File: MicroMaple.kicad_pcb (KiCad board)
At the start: 2 copper layers, 38.1 x 38.1 mm, 45 parts, among them P1 USB_OTG, P2 CONN_01X14, P3 CONN_01X14, P4 CONN_01X12, P5 CONN_01X01, P6 CONN_01X01, P7 CONN_01X01, P8 CONN_01X01, Q1 8050, Q2 8050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

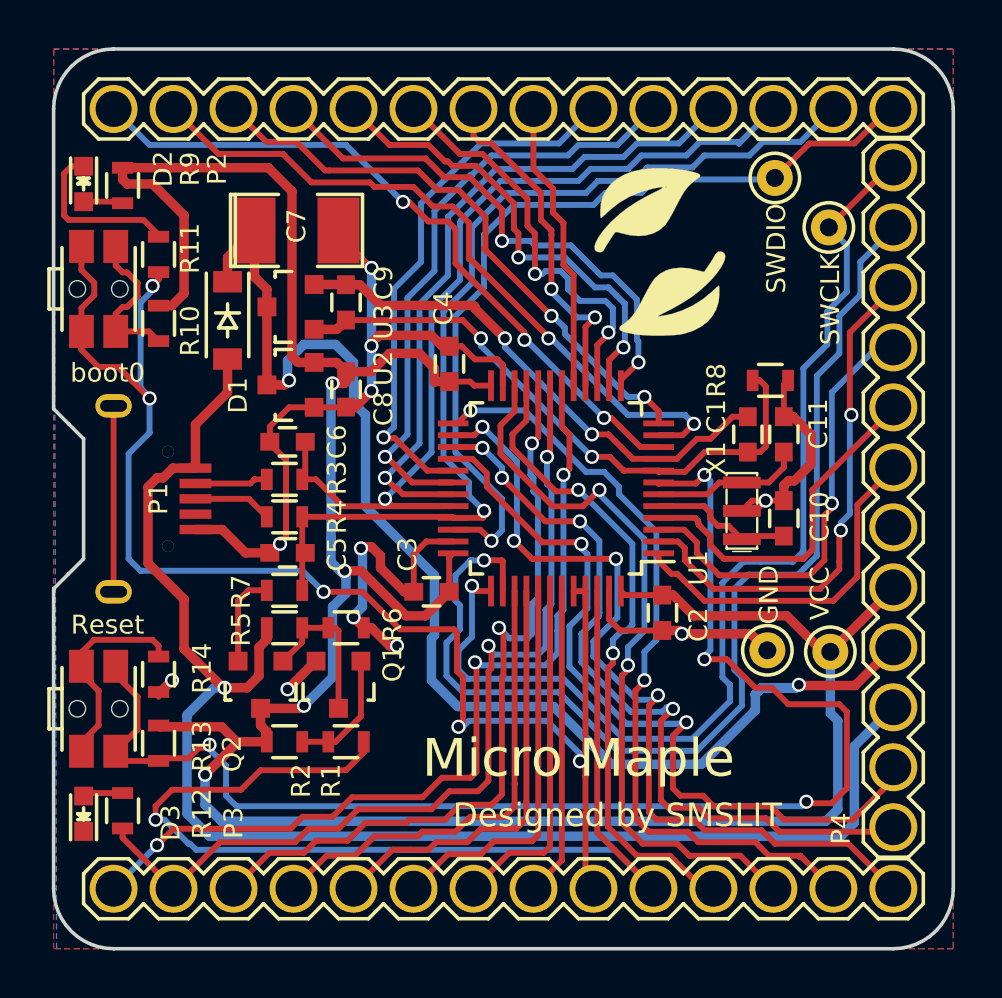
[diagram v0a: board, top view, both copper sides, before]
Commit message: 1.remove the USB disconnect circuit. 2.export v1.1 pdf. 3.add smslit logo lib
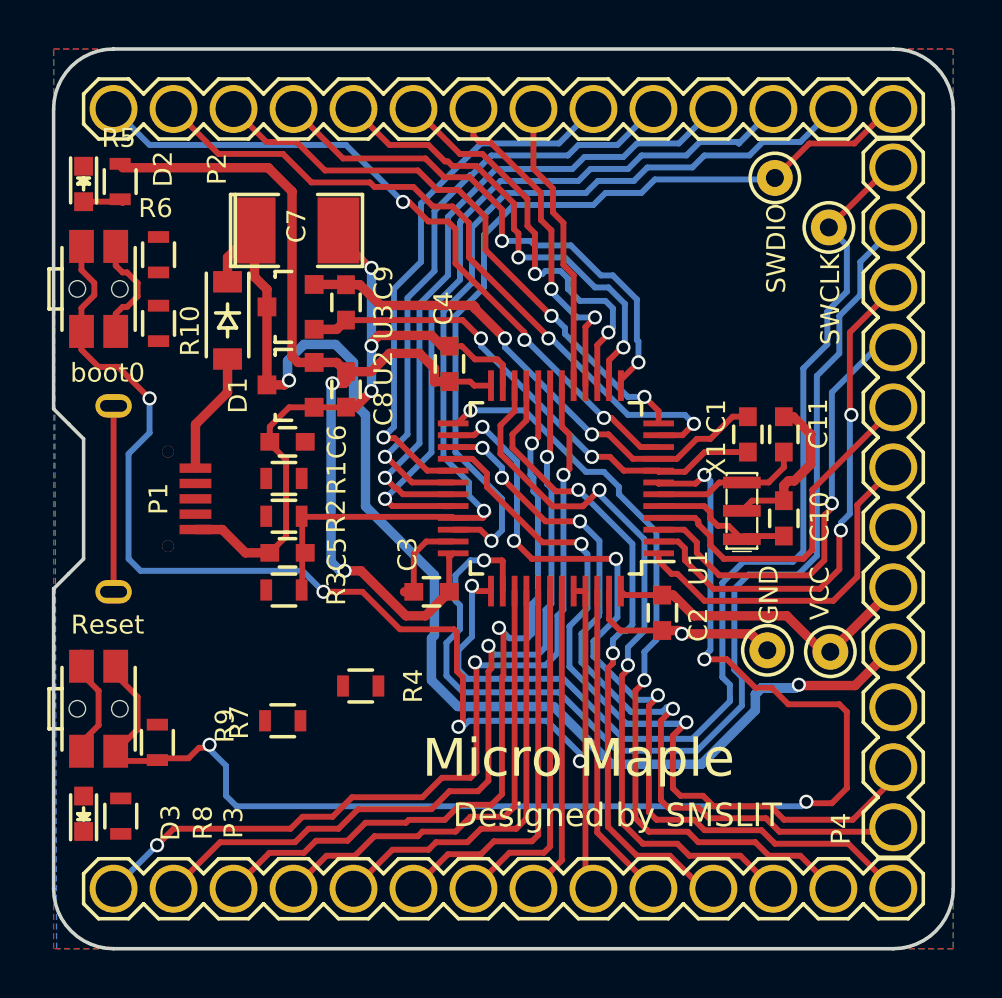
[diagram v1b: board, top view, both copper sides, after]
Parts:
- removed G***: LOGO, myFootprints:logo
- removed Q1, Q2: 8050, TO_SOT_Packages_SMD:SOT-23
- removed R11, R13: 10K, Resistors_SMD:R_0603
- removed R12, R14: 1K, Resistors_SMD:R_0603
- R1: value 1K -> 22
- R2: value 47K -> 22
- R3: value 22 -> 1.5K
- R4: value 22 -> 0
- R5: value 10K -> 1K
- R6: value 36K -> 1K
- R7: value 1.5K -> 10K
- R8: value 0 -> 1K
- R9: value 1K -> 10K
- moved R8 33.1 mm to (132.4, 123.9), turned to 270 degrees
- moved R9 23.6 mm to (133.9, 120.8)
- moved R5 20.1 mm to (132.4, 97.1), turned to 90 degrees
- moved R6 17.7 mm to (134.0, 100.2), turned to 270 degrees
- moved R1 11.5 mm to (139.3, 109.6)
- moved R2 9.55 mm to (139.3, 111.2)
- moved R4 7.86 mm to (142.5, 118.4)
- moved R7 5.53 mm to (139.2, 119.9)
- moved R3 4.69 mm to (139.3, 114.4)
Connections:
- R1 pad 1: /PB9 -> /PA11
- R1 pad 2: Net-(Q1-Pad1) -> Net-(P1-Pad2)
- R10 pad 1: VCC -> Net-(R10-Pad1)
- R10 pad 2: Net-(R10-Pad2) -> GND
- R2 pad 1: Net-(Q1-Pad1) -> /PA12
- R2 pad 2: VCC -> Net-(P1-Pad3)
- R3 pad 1: /PA11 -> /PA12
- R3 pad 2: Net-(P1-Pad2) -> VCC
- R4 pad 1: /PA12 -> GND
- R4 pad 2: Net-(P1-Pad3) -> GNDA
- R5 pad 1: Net-(Q1-Pad3) -> Net-(D2-Pad2)
- R5 pad 2: +5V -> VCC
- R6 pad 1: GND -> VCC
- R6 pad 2: Net-(Q1-Pad3) -> Net-(R6-Pad2)
- R7 pad 1: /PA12 -> GND
- R7 pad 2: Net-(Q2-Pad2) -> /PB8
- R8 pad 1: GND -> Net-(D3-Pad2)
- R8 pad 2: GNDA -> /PB1
- R9 pad 1: Net-(D2-Pad2) -> /RST
- SW1 pad 1: Net-(R10-Pad2) -> Net-(R6-Pad2)
- SW2 pad 2: Net-(R14-Pad1) -> Net-(R10-Pad1)
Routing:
- net VCC: track 116.0 -> 55.5 mm, vias 4 -> 2
- net +5V: track 63.4 -> 6.62 mm, vias 1 -> 0
- net /PB9: track 47.0 -> 13.6 mm, vias 1 -> 0
- net GND: track 70.3 -> 48.8 mm, vias 11 -> 4
- net Net-(R14-Pad1): track 8.84 -> 0.00 mm
- net /PA11: track 40.1 -> 31.9 mm
- net Net-(Q1-Pad3): track 6.62 -> 0.00 mm
- net Net-(R10-Pad2): track 6.58 -> 0.00 mm
- net /PB8: track 61.2 -> 54.8 mm, vias 5 -> 4
- net Net-(Q1-Pad1): track 5.27 -> 0.00 mm
- net Net-(R10-Pad1): track 0.00 -> 4.79 mm
- net Net-(R6-Pad2): track 0.00 -> 4.59 mm
- net GNDA: track 25.8 -> 21.8 mm
- net Net-(Q2-Pad2): track 3.96 -> 0.00 mm
- net /PB1: track 39.1 -> 35.6 mm
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
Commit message: add the pinmap xlsx file and encorrect the Bsilks text for pins.
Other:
- board text added: "PB15 MOSI2"
- board text added: "PB6/PWM/SCL1"
- board text added: "PB7/PWM/SDA1"
- board text removed: "PB15 MISO2"
- board text removed: "PB6/PWM/SDA1"
- board text removed: "PB7/PWM/SCL1"
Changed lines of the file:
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@@
     (links 111)
     (no_connects 24)
-    (area 120.826799 86.2 178.03 129.615001)
+    (area 129.464999 91.364999 167.715001 129.615001)
     (thickness 1.6)
     (drawings 185)
@@
     (34 B.Paste user)
     (35 F.Paste user)
-    (36 B.SilkS user hide)
+    (36 B.SilkS user)
     (37 F.SilkS user)
     (38 B.Mask user)
@@
   (gr_line (start 155.702 119.507) (end 158.877 122.682) (angle 90) (layer B.SilkS) (width 0.2))
   (gr_line (start 155.702 112.268) (end 155.702 119.507) (angle 90) (layer B.SilkS) (width 0.2))
-  (gr_text "PB15\nMISO2" (at 160.147 120.142 90) (layer B.SilkS)
+  (gr_text "PB15\nMOSI2" (at 160.147 120.142 90) (layer B.SilkS)
     (effects (font (size 0.8 0.8) (thickness 0.12)) (justify mirror))
   )
@@
     (effects (font (size 0.8 0.8) (thickness 0.12)) (justify mirror))
   )
-  (gr_text PB7/PWM/SCL1 (at 142.24 114.808 90) (layer B.SilkS)
+  (gr_text PB7/PWM/SDA1 (at 142.24 114.808 90) (layer B.SilkS)
     (effects (font (size 0.8 0.8) (thickness 0.12)) (justify mirror))
   )
-  (gr_text PB6/PWM/SDA1 (at 139.7 114.808 90) (layer B.SilkS)
+  (gr_text PB6/PWM/SCL1 (at 139.7 114.808 90) (layer B.SilkS)
     (effects (font (size 0.8 0.8) (thickness 0.12)) (justify mirror))
   )

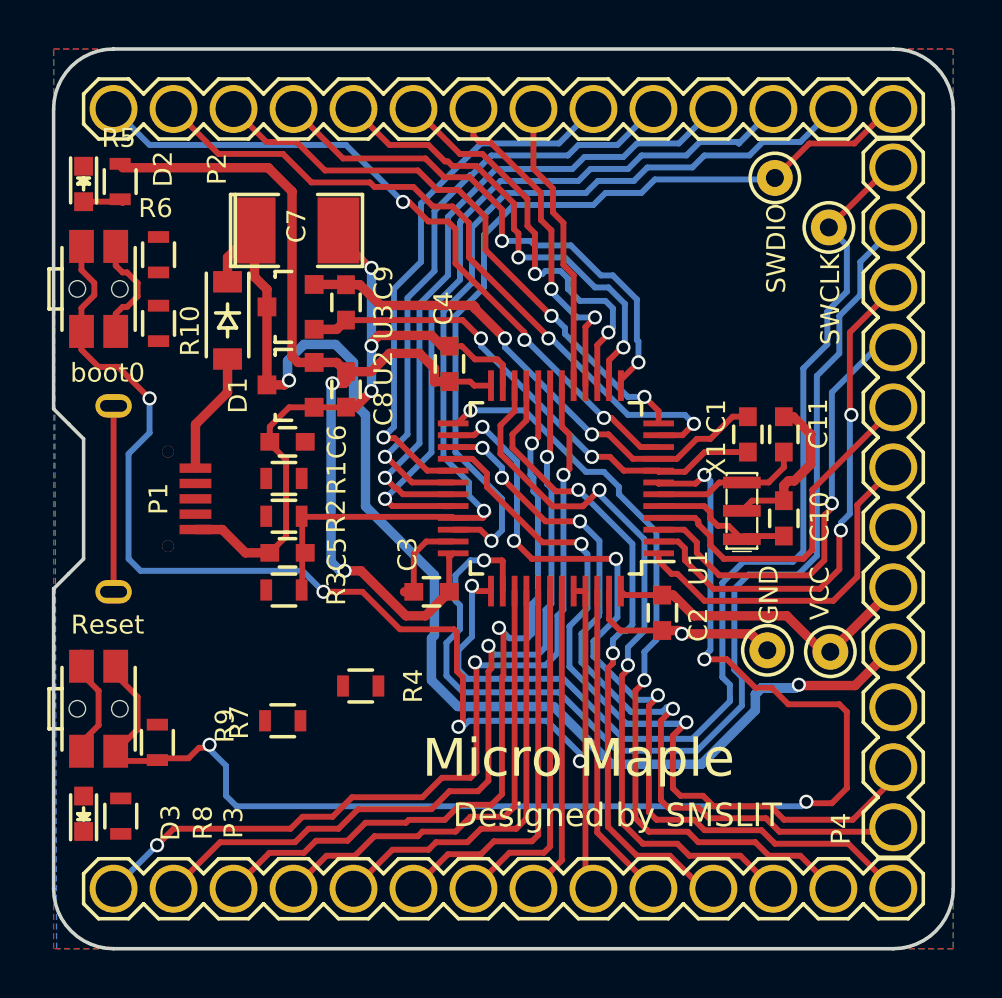
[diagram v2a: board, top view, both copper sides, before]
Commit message: Micro Maple Version1.1 : 1. update the sch and netlist file; 2. finish pcb trace layout
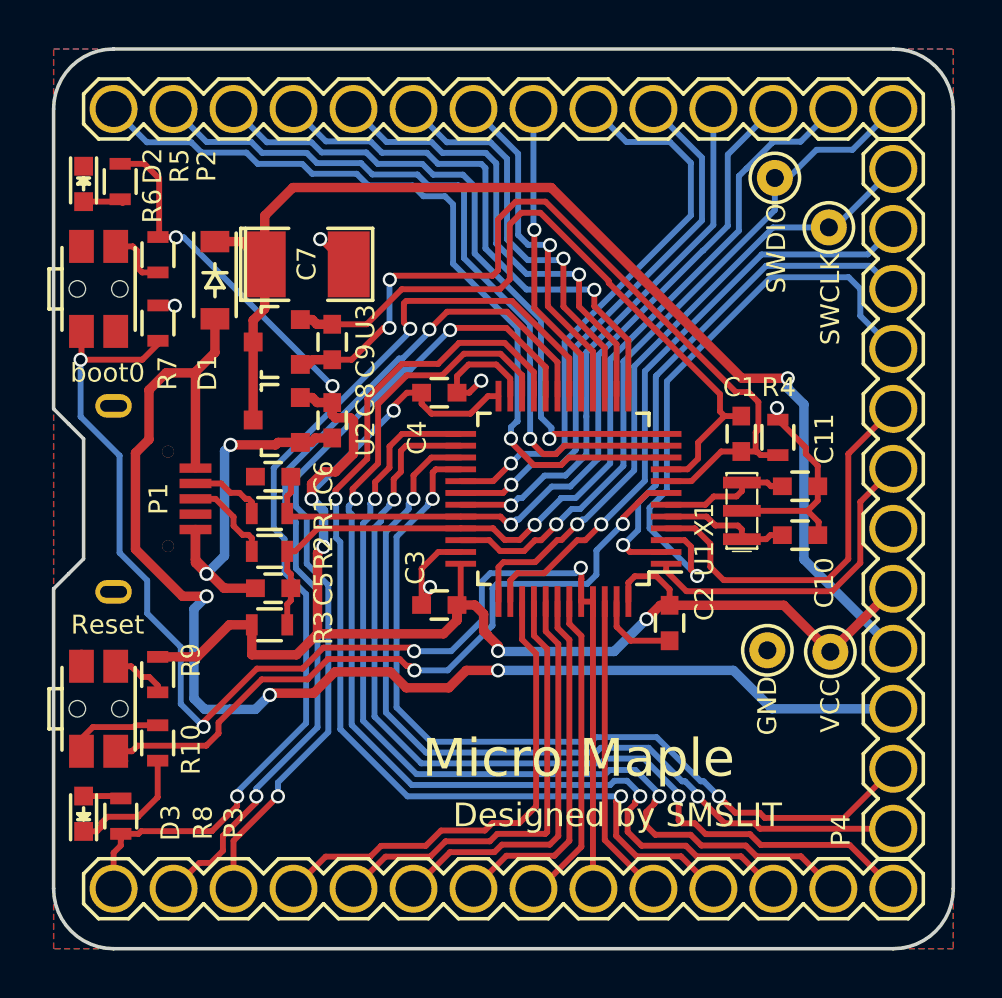
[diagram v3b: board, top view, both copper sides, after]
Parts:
- moved R4 20.6 mm to (160.2, 107.9), turned to 270 degrees
- moved R10 17.8 mm to (133.9, 120.8)
- moved R7 17.6 mm to (134.0, 103.0), turned to 270 degrees
- moved R9 2.87 mm to (133.9, 117.9)
- moved C11 2.30 mm to (161.2, 110.0), turned to 180 degrees
- moved D1 1.78 mm to (136.4, 101.2)
- moved C9 1.78 mm to (141.3, 103.8)
- moved C5 1.62 mm to (138.8, 114.3)
- moved R1 1.61 mm to (138.7, 111.1)
- moved R2 1.61 mm to (138.7, 112.7)
- moved U2 1.60 mm to (139.0, 107.1)
- moved U3 1.60 mm to (139.0, 103.8)
- moved C6 1.59 mm to (138.8, 109.6)
- moved R3 1.59 mm to (138.7, 115.8)
- moved C7 1.50 mm to (140.3, 100.6)
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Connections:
- R8 pad 2: /PB1 -> /PB0
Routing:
- net +5V: track 6.62 -> 56.4 mm, vias 0 -> 3
- net VCC: track 55.5 -> 84.4 mm, vias 2 -> 7
- net /RST: track 58.9 -> 33.9 mm, vias 4 -> 2
- net /PA15: track 47.1 -> 26.0 mm
- net /PA14: track 45.8 -> 27.7 mm
- net /PB10: track 27.8 -> 44.1 mm
- net /PB11: track 31.4 -> 46.0 mm
- net GNDA: track 21.8 -> 35.7 mm
- net Net-(P1-Pad6): track 7.87 -> 0.00 mm
- net VDDA: track 22.6 -> 29.9 mm, vias 2 -> 0
- net /PB12: track 33.3 -> 39.9 mm
- net /PC14: track 19.0 -> 25.2 mm
- net /PA13: track 35.8 -> 29.8 mm
- net /PB0: track 37.6 -> 43.3 mm, vias 3 -> 2
- net /PA10: track 28.5 -> 23.1 mm
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
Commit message: V1.1: update the pcb desgin
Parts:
- added G***: LOGO, myFootprints:logo, F.Cu at (153.7, 100.0)
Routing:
- net GND: track 47.8 -> 73.9 mm, vias 7 -> 9
- net +BATT: track 50.7 -> 56.3 mm
- net VDDA: track 29.9 -> 32.0 mm
- net GNDA: track 35.7 -> 37.4 mm
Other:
- board text added: "Micro Maple V1.1"
- board text removed: "Micro Maple"

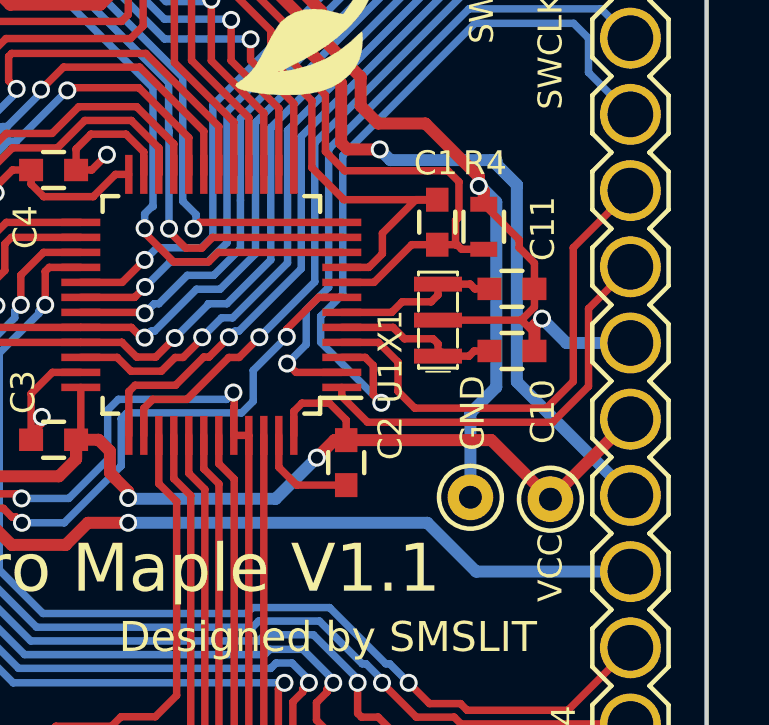
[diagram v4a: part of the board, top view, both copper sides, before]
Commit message: because the mistake in m2OLED pcb design, change the position of GND\VCC\VBAT
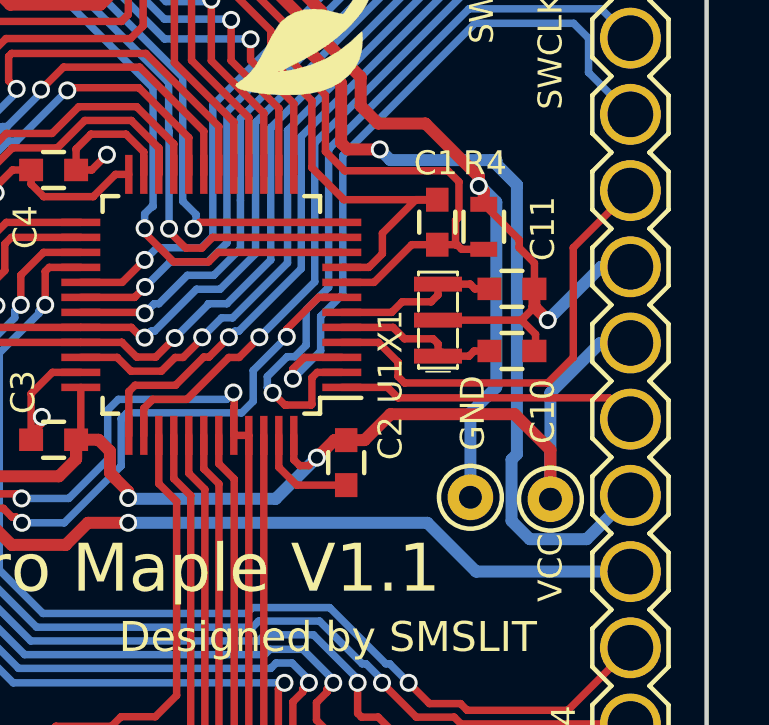
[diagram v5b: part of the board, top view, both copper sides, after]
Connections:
- P4 pad 6: /VBAT -> GND
- P4 pad 7: GND -> VCC
- P4 pad 8: VCC -> /VBAT
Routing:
- net +BATT: track 56.3 -> 60.4 mm
- net /VBAT: track 13.9 -> 10.1 mm
- net VCC: track 84.4 -> 87.4 mm
- net /PC13: track 22.1 -> 25.0 mm
- net /PC14: track 25.2 -> 23.6 mm
- net /PC15: track 16.7 -> 15.3 mm
